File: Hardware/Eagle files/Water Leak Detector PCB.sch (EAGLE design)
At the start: 28 parts, among them IC1 74AHCT125, J1 Sensor 1, J2 Sensor 2, J3 Servo

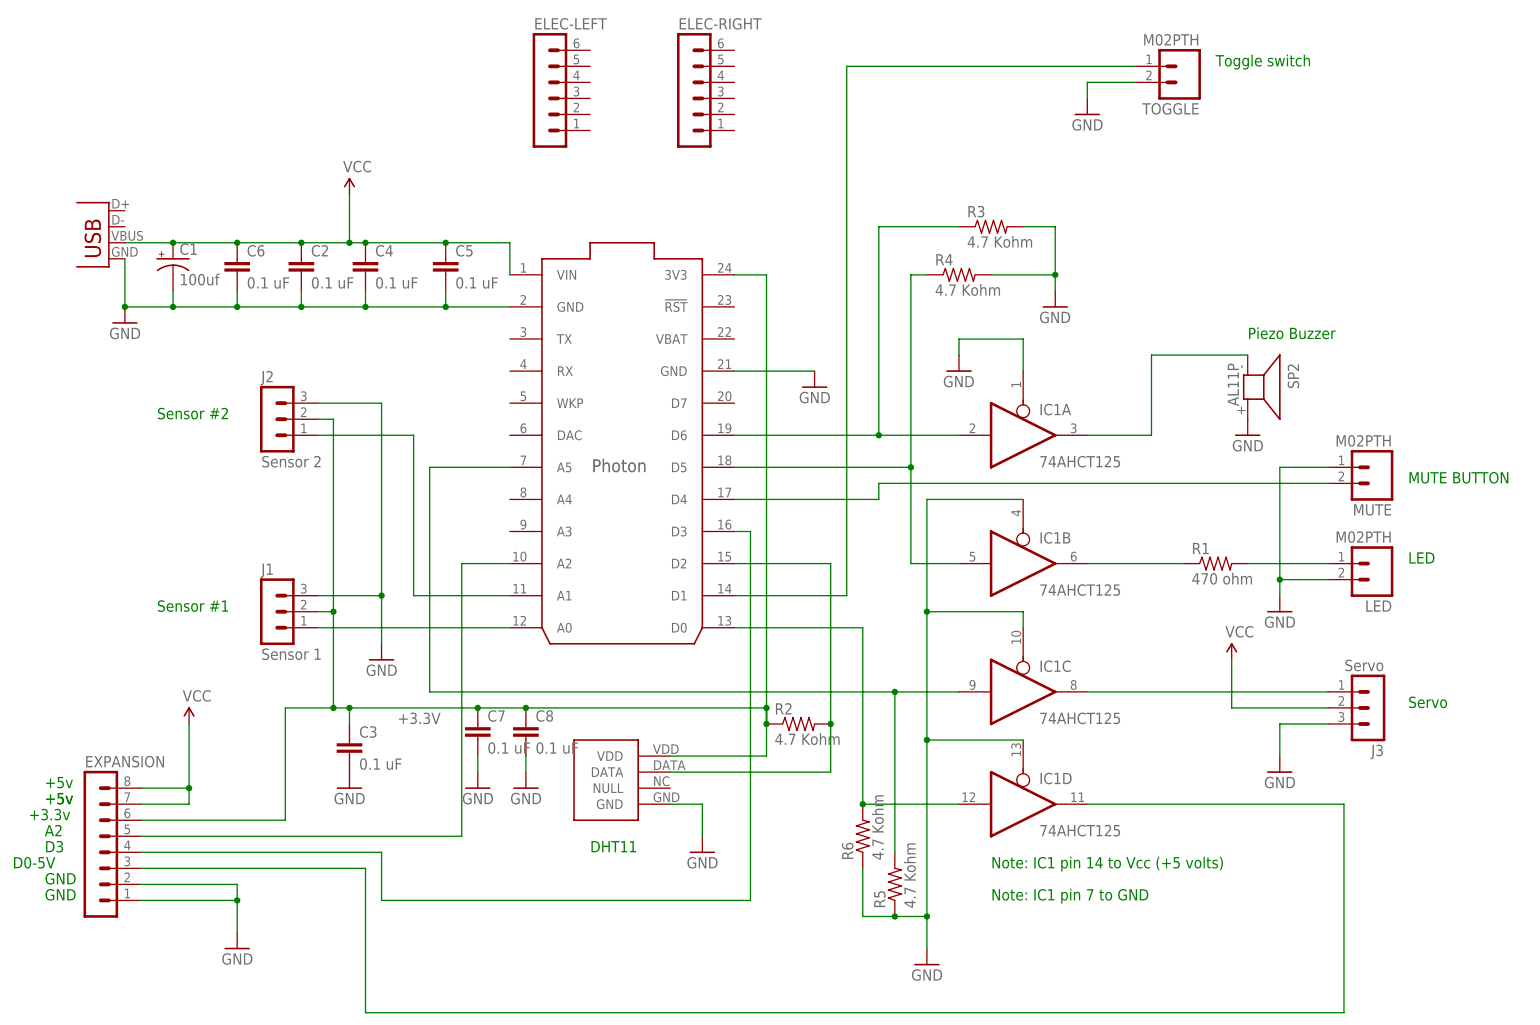
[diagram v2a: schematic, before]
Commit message: pcb v2. changed buzzer. adjusted position of J1-4 to align. Added much text to top silk.
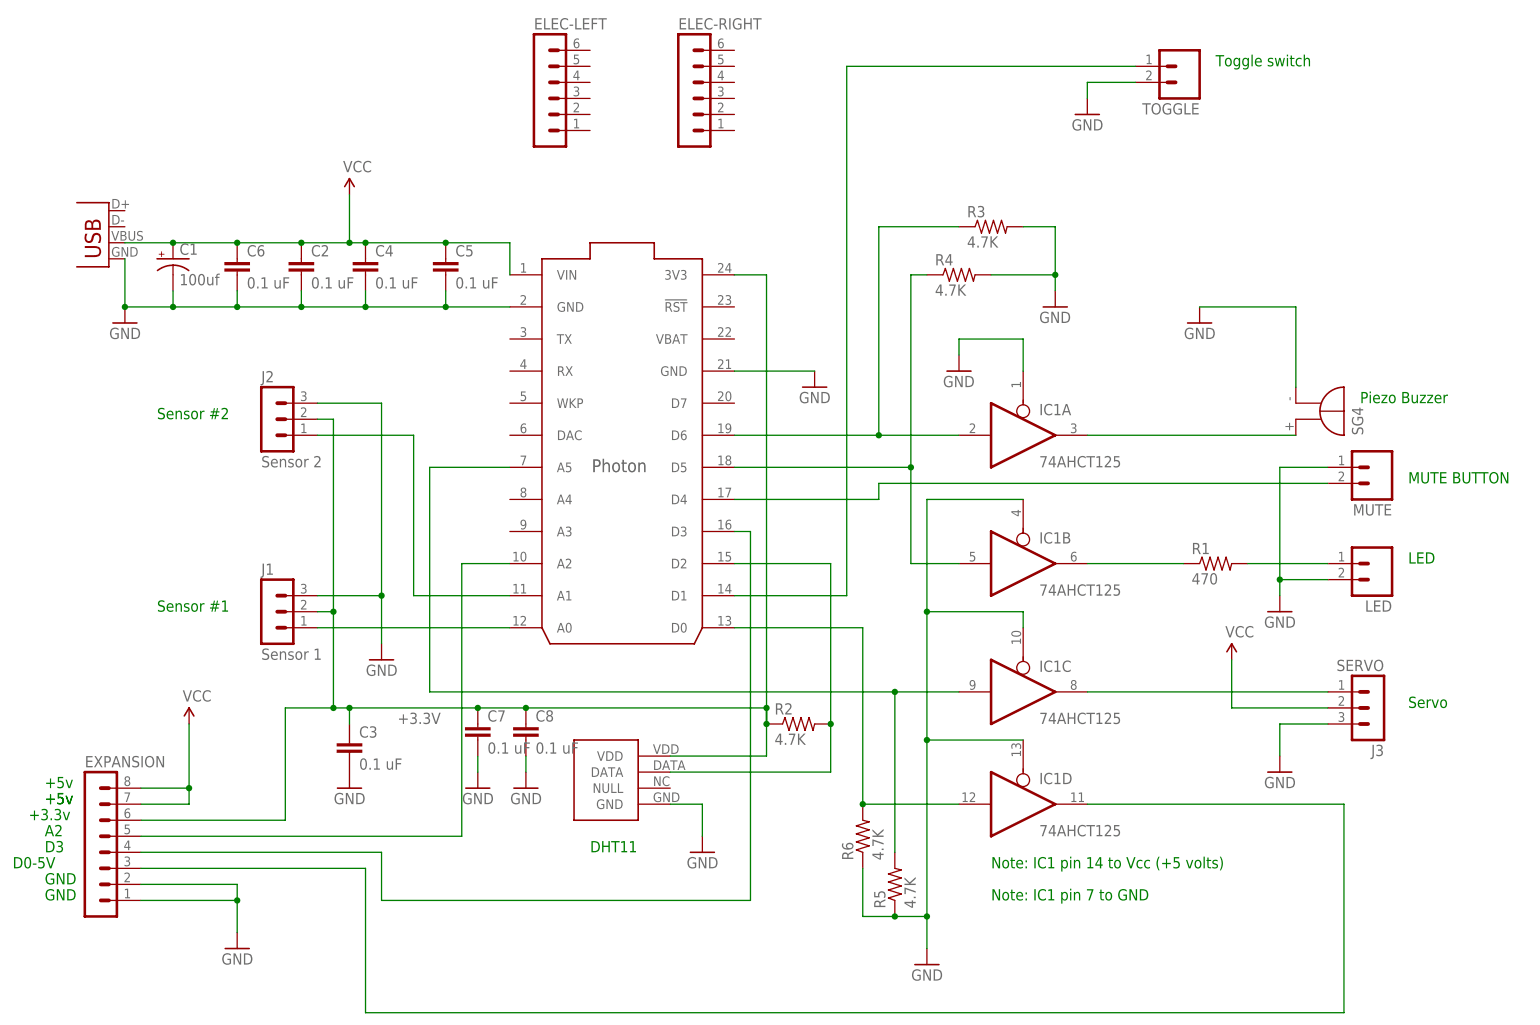
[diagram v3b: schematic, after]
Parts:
- removed SP2: AL11P, buzzer:AL11P
- added SG4: F/HMB, buzzer:F/HMB
- J3: value Servo -> SERVO
- R1: value 470 ohm -> 470
- R2, R3, R4, R5, R6: value 4.7 Kohm -> 4.7K
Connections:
- net GND: now also SG4.-; no longer SP2.2
- net N$6: now also SG4.+; no longer SP2.1
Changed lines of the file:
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@@
 <?xml version="1.0" encoding="utf-8"?>
 <!DOCTYPE eagle SYSTEM "eagle.dtd">
-<eagle version="7.4.0">
+<eagle version="8.2.1">
 <drawing>
 <settings>
@@
 <layers>
 <layer number="1" name="Top" color="4" fill="1" visible="no" active="no"/>
+<layer number="2" name="Route2" color="1" fill="3" visible="no" active="no"/>
+<layer number="3" name="Route3" color="4" fill="3" visible="no" active="no"/>
+<layer number="4" name="Route4" color="1" fill="4" visible="no" active="no"/>
+<layer number="5" name="Route5" color="4" fill="4" visible="no" active="no"/>
+<layer number="6" name="Route6" color="1" fill="8" visible="no" active="no"/>
+<layer number="7" name="Route7" color="4" fill="8" visible="no" active="no"/>
+<layer number="8" name="Route8" color="1" fill="2" visible="no" active="no"/>
+<layer number="9" name="Route9" color="4" fill="2" visible="no" active="no"/>
+<layer number="10" name="Route10" color="1" fill="7" visible="no" active="no"/>
+<layer number="11" name="Route11" color="4" fill="7" visible="no" active="no"/>
+<layer number="12" name="Route12" color="1" fill="5" visible="no" active="no"/>
+<layer number="13" name="Route13" color="4" fill="5" visible="no" active="no"/>
+<layer number="14" name="Route14" color="1" fill="6" visible="no" active="no"/>
+<layer number="15" name="Route15" color="4" fill="6" visible="no" active="no"/>
 <layer number="16" name="Bottom" color="1" fill="1" visible="no" active="no"/>
 <layer number="17" name="Pads" color="2" fill="1" visible="no" active="no"/>
@@
 <part name="GND3" library="SparkFun-Aesthetics" deviceset="GND" device=""/>
 <part name="IC1" library="74xx-us" deviceset="74*125" device="N" value="74AHCT125"/>
-<part name="R1" library="rcl" deviceset="R-US_" device="0309/12" value="470 ohm"/>
-<part name="SP2" library="buzzer" deviceset="AL11P" device=""/>
+<part name="R1" library="rcl" deviceset="R-US_" device="0309/12" value="470"/>
 <part name="GND5" library="SparkFun-Aesthetics" deviceset="GND" device=""/>
 <part name="U$2" library="Spark" deviceset="DHT22" device=""/>
@@
 <part name="GND7" library="SparkFun-Aesthetics" deviceset="GND" device=""/>
 <part name="SUPPLY1" library="SparkFun-Aesthetics" deviceset="VCC" device=""/>
-<part name="J3" library="con-lstb" deviceset="MA03-1" device="" value="Servo"/>
+<part name="J3" library="con-lstb" deviceset="MA03-1" device="" value="SERVO"/>
 <part name="SUPPLY2" library="SparkFun-Aesthetics" deviceset="VCC" device=""/>
 <part name="GND4" library="SparkFun-Aesthetics" deviceset="GND" device=""/>
 <part name="GND9" library="SparkFun-Aesthetics" deviceset="GND" device=""/>
-<part name="R2" library="rcl" deviceset="R-US_" device="0309/12" value="4.7 Kohm"/>
-<part name="R3" library="rcl" deviceset="R-US_" device="0309/12" value="4.7 Kohm"/>
-<part name="R4" library="rcl" deviceset="R-US_" device="0309/12" value="4.7 Kohm"/>
-<part name="R5" library="rcl" deviceset="R-US_" device="0309/12" value="4.7 Kohm"/>
-<part name="R6" library="rcl" deviceset="R-US_" device="0309/12" value="4.7 Kohm"/>
+<part name="R2" library="rcl" deviceset="R-US_" device="0309/12" value="4.7K"/>
+<part name="R3" library="rcl" deviceset="R-US_" device="0309/12" value="4.7K"/>
+<part name="R4" library="rcl" deviceset="R-US_" device="0309/12" value="4.7K"/>
+<part name="R5" library="rcl" deviceset="R-US_" device="0309/12" value="4.7K"/>
+<part name="R6" library="rcl" deviceset="R-US_" device="0309/12" value="4.7K"/>
 <part name="C4" library="SparkFun-Passives" deviceset="CAP" device="PTH" value="0.1 uF"/>
 <part name="C5" library="SparkFun-Passives" deviceset="CAP" device="PTH" value="0.1 uF"/>
@@
 <part name="ELEC-LEFT" library="con-lstb" deviceset="MA06-1" device=""/>
 <part name="ELEC-RIGHT" library="con-lstb" deviceset="MA06-1" device=""/>
-<part name="MUTE" library="SparkFun-Connectors" deviceset="M02" device="PTH"/>
-<part name="LED" library="SparkFun-Connectors" deviceset="M02" device="PTH"/>
-<part name="TOGGLE" library="SparkFun-Connectors" deviceset="M02" device="PTH"/>
+<part name="MUTE" library="SparkFun-Connectors" deviceset="M02" device="PTH" value=""/>
+<part name="LED" library="SparkFun-Connectors" deviceset="M02" device="PTH" value=""/>
+<part name="TOGGLE" library="SparkFun-Connectors" deviceset="M02" device="PTH" value=""/>
 <part name="C6" library="SparkFun-Passives" deviceset="CAP" device="PTH" value="0.1 uF"/>
 <part name="C7" library="SparkFun-Passives" deviceset="CAP" device="PTH" value="0.1 uF"/>
@@
 <part name="GND15" library="SparkFun-Aesthetics" deviceset="GND" device=""/>
 <part name="U$1" library="Spark" deviceset="PHOTON" device="_WITH_HEADERS"/>
+<part name="SG4" library="buzzer" library_urn="urn:adsk.eagle:library:113" deviceset="F/HMB" device="" value=""/>
 </parts>
 <sheets>
@@
 <text x="116.84" y="25.4" size="1.778" layer="91">Servo</text>
 <text x="50.8" y="0" size="1.778" layer="91">Note: IC1 pin 14 to Vcc (+5 volts)</text>
-<text x="91.44" y="83.82" size="1.778" layer="91">Piezo Buzzer</text>
+<text x="109.22" y="73.66" size="1.778" layer="91">Piezo Buzzer</text>
 <text x="50.8" y="-5.08" size="1.778" layer="91">Note: IC1 pin 7 to GND</text>
 <text x="86.36" y="127" size="1.778" layer="91">Toggle switch</text>
@@
 <instance part="IC1" gate="D" x="55.88" y="10.16"/>
 <instance part="R1" gate="G$1" x="86.36" y="48.26"/>
-<instance part="SP2" gate="G$1" x="91.44" y="76.2" rot="R270"/>
 <instance part="GND5" gate="1" x="40.64" y="-15.24" rot="MR0"/>
 <instance part="U$2" gate="G$1" x="-15.24" y="7.62"/>
@@
 <instance part="J3" gate="G$1" x="111.76" y="25.4" rot="R180"/>
 <instance part="SUPPLY2" gate="1" x="88.9" y="33.02"/>
-<instance part="GND4" gate="1" x="91.44" y="68.58" rot="MR0"/>
+<instance part="GND4" gate="1" x="83.82" y="86.36" rot="MR0"/>
 <instance part="GND9" gate="1" x="22.86" y="76.2" rot="MR0"/>
 <instance part="R2" gate="G$1" x="20.32" y="22.86"/>
@@
 <instance part="GND15" gate="1" x="-22.86" y="12.7" rot="MR0"/>
 <instance part="U$1" gate="G$1" x="-7.62" y="66.04"/>
+<instance part="SG4" gate="G$1" x="101.6" y="71.12" rot="MR90"/>
 </instances>
 <busses>
@@
 </segment>
 <segment>
-<pinref part="SP2" gate="G$1" pin="2"/>
-<pinref part="GND4" gate="1" pin="GND"/>
-</segment>
-<segment>
 <pinref part="C3" gate="G$1" pin="2"/>
 <pinref part="GND3" gate="1" pin="GND"/>
@@
 <pinref part="GND15" gate="1" pin="GND"/>
 <wire x1="-22.86" y1="17.78" x2="-22.86" y2="15.24" width="0.1524" layer="91"/>
+</segment>
+<segment>
+<pinref part="GND4" gate="1" pin="GND"/>
+<wire x1="83.82" y1="88.9" x2="99.06" y2="88.9" width="0.1524" layer="91"/>
+<pinref part="SG4" gate="G$1" pin="-"/>
+<wire x1="99.06" y1="88.9" x2="99.06" y2="76.2" width="0.1524" layer="91"/>
 </segment>
 </net>
@@
 <net name="N$6" class="0">
 <segment>
-<wire x1="76.2" y1="68.58" x2="76.2" y2="81.28" width="0.1524" layer="91"/>
-<pinref part="SP2" gate="G$1" pin="1"/>
-<wire x1="76.2" y1="81.28" x2="91.44" y2="81.28" width="0.1524" layer="91"/>
 <pinref part="IC1" gate="A" pin="O"/>
-<wire x1="66.04" y1="68.58" x2="76.2" y2="68.58" width="0.1524" layer="91"/>
+<wire x1="66.04" y1="68.58" x2="99.06" y2="68.58" width="0.1524" layer="91"/>
+<pinref part="SG4" gate="G$1" pin="+"/>
 </segment>
 </net>
@@
 </sheet>
 </sheets>
+<errors>
+</errors>
 </schematic>
 </drawing>
@@
 which will not be processed correctly with this version.
 </note>
+<note version="8.2" severity="warning">
+Since Version 8.2, Eagle supports online libraries. The ids
+of those online libraries will not be understood (or retained)
+with this version.
+</note>
 </compatibility>
